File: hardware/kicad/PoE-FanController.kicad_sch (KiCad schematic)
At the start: 32 parts, among them J2 FAN1, J3 FAN2, J4 FAN3, J5 FAN4, J6 Molex_KK254_3pin, J8 Waveshare_ESP32P4POEETH, U1 LM2587-12

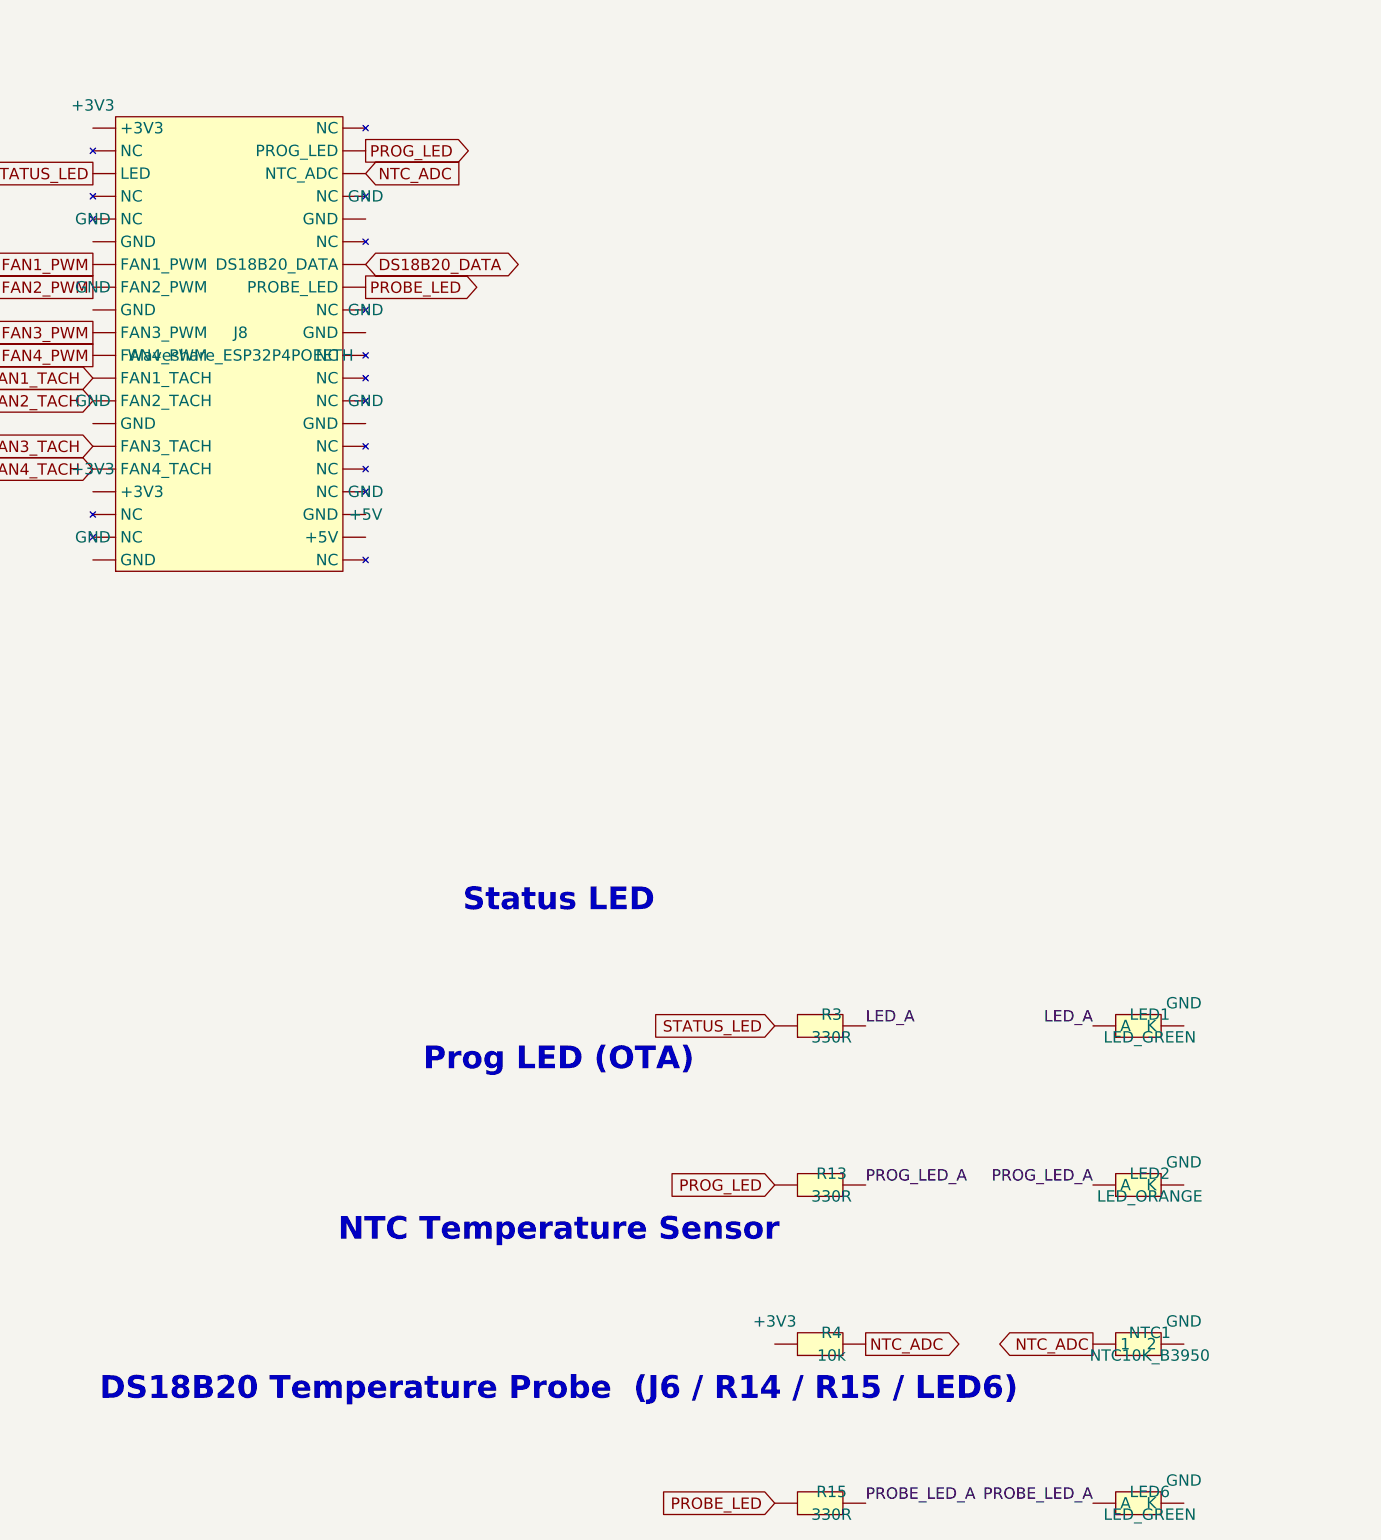
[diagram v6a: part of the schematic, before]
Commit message: feat(hw): replace NTC1/R4 with DHT11 breakout in schematic generator (#135)
- Remove Custom:NTC symbol definition from components.py
- Add Custom:DHT11_Breakout 3-pin symbol (VCC/DATA/GND)
- Remove R4 (NTC bias resistor) component and wiring
- Remove NTC1 thermistor component and wiring
- Add HUM1 (DHT11_Breakout) at same schematic row
- Rename NTC_ADC net to DHT11_DATA on J8 pin 23 (GPIO16)
- Update bom.py: remove R4/NTC1 rows, add HUM1 row
- ERC: 0 errors, 79 warnings (pre-existing)

Closes #135
Task: T001
Issue: #135

Co-authored-by: Copilot <223556219+Copilot@users.noreply.github.com>
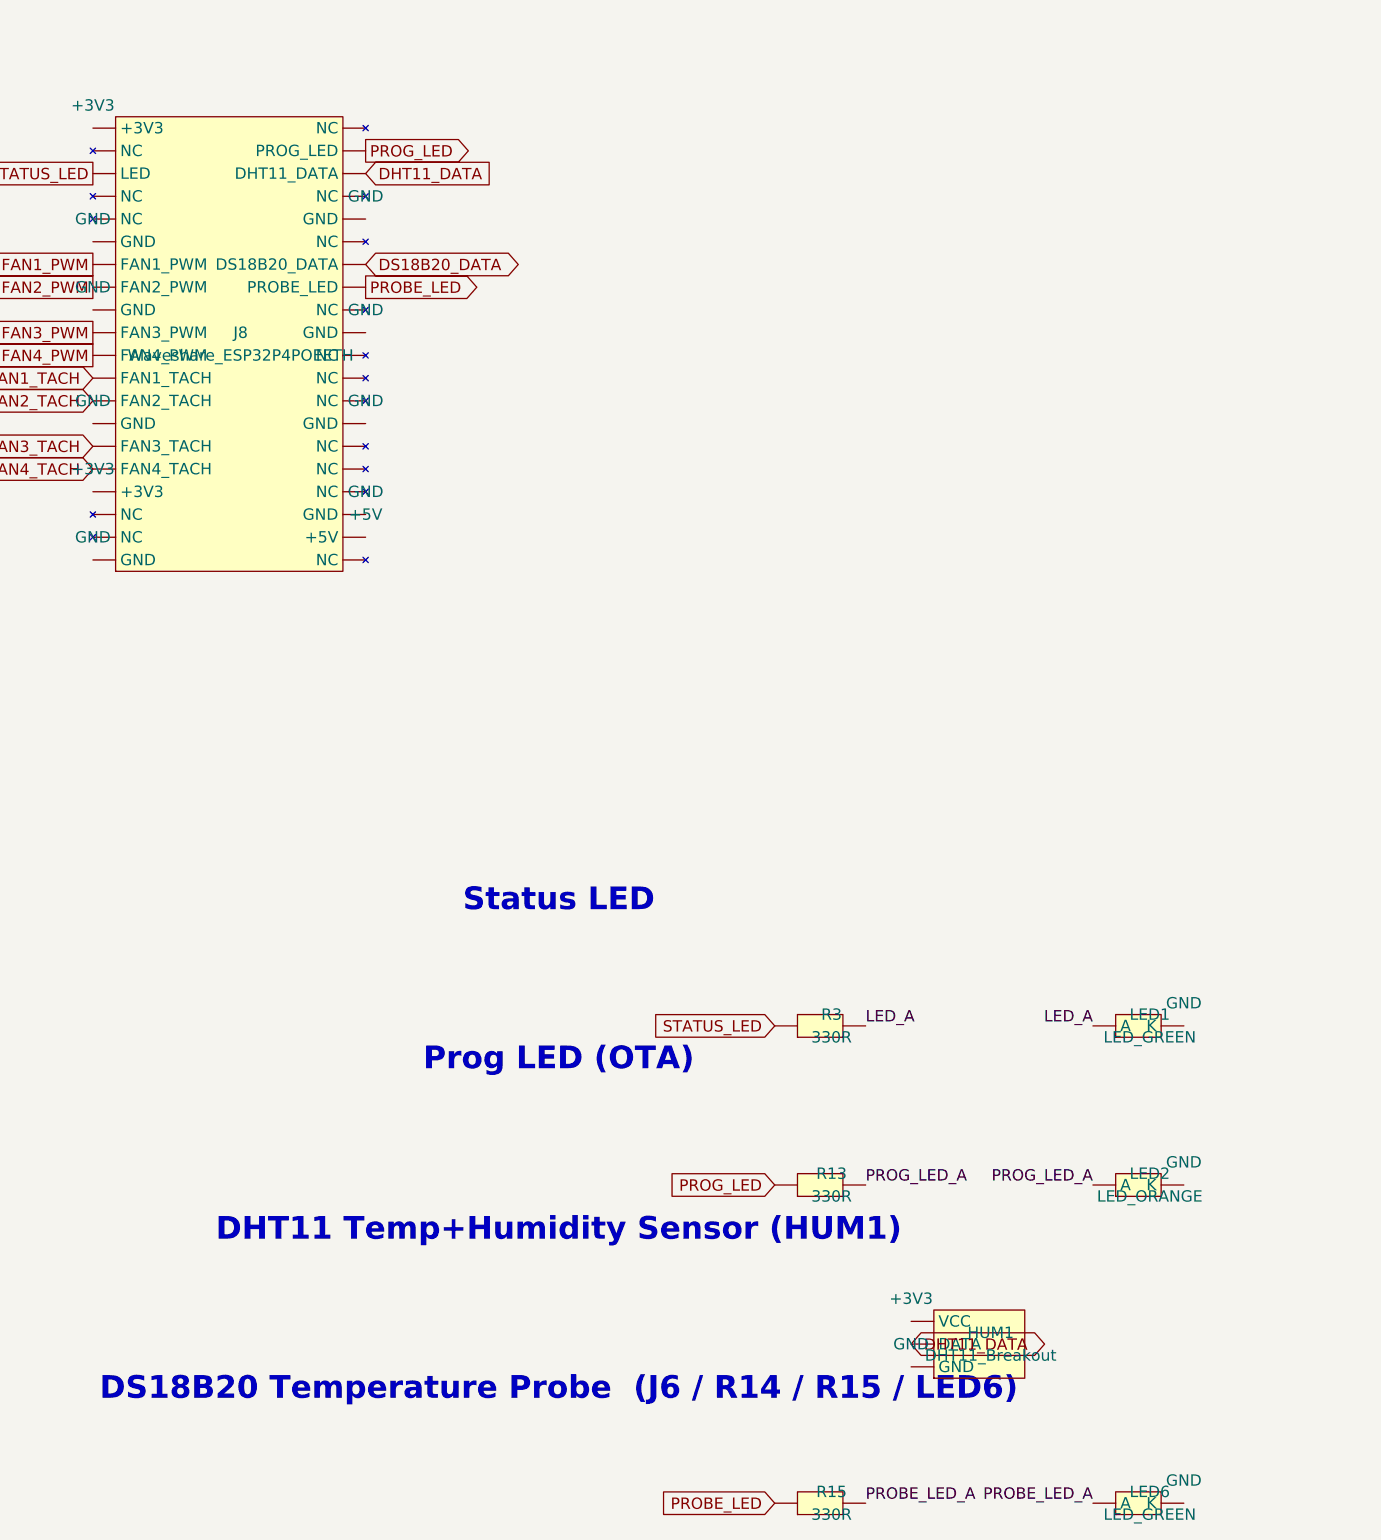
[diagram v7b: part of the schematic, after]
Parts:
- removed NTC1: NTC10K_B3950, Resistor_THT:R_Axial_DIN0207_L6.3mm_D2.5mm_P10.16mm_Horizontal, symbol Custom:NTC
- removed R4: 10k, Resistor_THT:R_Axial_DIN0207_L6.3mm_D2.5mm_P7.62mm_Horizontal, symbol Custom:R
- added HUM1: DHT11_Breakout, Connector_PinHeader_2.54mm:PinHeader_1x03_P2.54mm_Vertical, symbol Custom:DHT11_Breakout
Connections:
- net NTC_ADC renamed DHT11_DATA
- net DHT11_DATA: now also HUM1.2 (DATA)
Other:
- note added: "DHT11 Temp+Humidity Sensor (HUM1)"
- note removed: "NTC Temperature Sensor"
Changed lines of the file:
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@@
     (instances (project "PoE-FanController" (path "/" (reference "#PWR031") (unit 1))))
   )
-  (text "NTC Temperature Sensor" (at 128.2700 251.4600 0)
+  (text "DHT11 Temp+Humidity Sensor (HUM1)" (at 128.2700 251.4600 0)
     (effects (font (color 0 0 255 1) (bold yes) (size 2.54 2.54)))
 )
-  (symbol (lib_id "Custom:R") (at 157.4800 264.1600 0)
-    (unit 1) (exclude_from_sim no) (in_bom yes) (on_board yes) (dnp no)
-    (property "Reference" "R4"
-      (at 158.7500 262.8900 0)
-      (effects (font (size 1.27 1.27))))
-    (property "Value" "10k"
-      (at 158.7500 265.4300 0)
-      (effects (font (size 1.27 1.27))))
-    (property "Footprint" "Resistor_THT:R_Axial_DIN0207_L6.3mm_D2.5mm_P7.62mm_Horizontal"
-      (at 157.4800 264.1600 0)
+  (symbol (lib_id "Custom:DHT11_Breakout") (at 175.2600 264.1600 0)
+    (unit 1) (exclude_from_sim no) (in_bom yes) (on_board yes) (dnp no)
+    (property "Reference" "HUM1"
+      (at 176.5300 262.8900 0)
+      (effects (font (size 1.27 1.27))))
+    (property "Value" "DHT11_Breakout"
+      (at 176.5300 265.4300 0)
+      (effects (font (size 1.27 1.27))))
+    (property "Footprint" "Connector_PinHeader_2.54mm:PinHeader_1x03_P2.54mm_Vertical"
+      (at 175.2600 264.1600 0)
       (hide yes)
       (effects (font (size 1.27 1.27))))
     (property "Datasheet" "~"
-      (at 157.4800 264.1600 0)
+      (at 175.2600 264.1600 0)
       (hide yes)
       (effects (font (size 1.27 1.27))))
     (pin "1")
     (pin "2")
-    (instances (project "PoE-FanController" (path "/" (reference "R4") (unit 1))))
-  )
-  (symbol (lib_id "power:+3V3") (at 152.4000 264.1600 0)
+    (pin "3")
+    (instances (project "PoE-FanController" (path "/" (reference "HUM1") (unit 1))))
+  )
+  (symbol (lib_id "power:+3V3") (at 167.6400 261.6200 0)
     (unit 1) (exclude_from_sim no) (in_bom yes) (on_board yes) (dnp no)
     (fields_autoplaced yes)
     (property "Reference" "#PWR032"
-      (at 152.4000 266.7000 0)
+      (at 167.6400 264.1600 0)
       (hide yes)
       (effects (font (size 1.27 1.27))))
     (property "Value" "+3V3"
-      (at 152.4000 261.6200 0)
-      (effects (font (size 1.27 1.27))))
-    (property "Footprint" ""
-      (at 152.4000 264.1600 0)
-      (hide yes)
-      (effects (font (size 1.27 1.27))))
-    (property "Datasheet" ""
-      (at 152.4000 264.1600 0)
+      (at 167.6400 259.0800 0)
+      (effects (font (size 1.27 1.27))))
+    (property "Footprint" ""
+      (at 167.6400 261.6200 0)
+      (hide yes)
+      (effects (font (size 1.27 1.27))))
+    (property "Datasheet" ""
+      (at 167.6400 261.6200 0)
       (hide yes)
       (effects (font (size 1.27 1.27))))
@@
     (instances (project "PoE-FanController" (path "/" (reference "#PWR032") (unit 1))))
   )
-  (global_label "NTC_ADC"
-    (shape output)
-    (at 162.5600 264.1600 0)
+  (global_label "DHT11_DATA"
+    (shape bidirectional)
+    (at 167.6400 264.1600 0)
     (fields_autoplaced yes)
     (effects (font (size 1.27 1.27)) (justify left))
     (property "Intersheetrefs" "${INTERSHEET_REFS}"
-      (at 170.1800 264.1600 0)
+      (at 175.2600 264.1600 0)
       (effects (font (size 1.27 1.27)) (justify left) (hide yes)))
   )
-  (symbol (lib_id "Custom:NTC") (at 193.0400 264.1600 0)
-    (unit 1) (exclude_from_sim no) (in_bom yes) (on_board yes) (dnp no)
-    (property "Reference" "NTC1"
-      (at 194.3100 262.8900 0)
-      (effects (font (size 1.27 1.27))))
-    (property "Value" "NTC10K_B3950"
-      (at 194.3100 265.4300 0)
-      (effects (font (size 1.27 1.27))))
-    (property "Footprint" "Resistor_THT:R_Axial_DIN0207_L6.3mm_D2.5mm_P10.16mm_Horizontal"
-      (at 193.0400 264.1600 0)
-      (hide yes)
-      (effects (font (size 1.27 1.27))))
-    (property "Datasheet" "~"
-      (at 193.0400 264.1600 0)
-      (hide yes)
-      (effects (font (size 1.27 1.27))))
-    (pin "1")
-    (pin "2")
-    (instances (project "PoE-FanController" (path "/" (reference "NTC1") (unit 1))))
-  )
-  (global_label "NTC_ADC"
-    (shape output)
-    (at 187.9600 264.1600 180)
-    (fields_autoplaced yes)
-    (effects (font (size 1.27 1.27)) (justify right))
-    (property "Intersheetrefs" "${INTERSHEET_REFS}"
-      (at 195.5800 264.1600 180)
-      (effects (font (size 1.27 1.27)) (justify right) (hide yes)))
-  )
-  (symbol (lib_id "power:GND") (at 198.1200 264.1600 0)
+  (symbol (lib_id "power:GND") (at 167.6400 266.7000 0)
     (unit 1) (exclude_from_sim no) (in_bom yes) (on_board yes) (dnp no)
     (fields_autoplaced yes)
     (property "Reference" "#PWR033"
-      (at 198.1200 266.7000 0)
-      (hide yes)
-      (effects (font (size 1.27 1.27))))
-    (property "Value" "GND"
-      (at 198.1200 261.6200 0)
-      (effects (font (size 1.27 1.27))))
-    (property "Footprint" ""
-      (at 198.1200 264.1600 0)
-      (hide yes)
-      (effects (font (size 1.27 1.27))))
-    (property "Datasheet" ""
-      (at 198.1200 264.1600 0)
+      (at 167.6400 269.2400 0)
+      (hide yes)
+      (effects (font (size 1.27 1.27))))
+    (property "Value" "GND"
+      (at 167.6400 264.1600 0)
+      (effects (font (size 1.27 1.27))))
+    (property "Footprint" ""
+      (at 167.6400 266.7000 0)
+      (hide yes)
+      (effects (font (size 1.27 1.27))))
+    (property "Datasheet" ""
+      (at 167.6400 266.7000 0)
       (hide yes)
       (effects (font (size 1.27 1.27))))
@@
       (effects (font (size 1.27 1.27)) (justify left) (hide yes)))
   )
-  (global_label "NTC_ADC"
+  (global_label "DHT11_DATA"
     (shape input)
     (at 106.6800 133.3500 0)

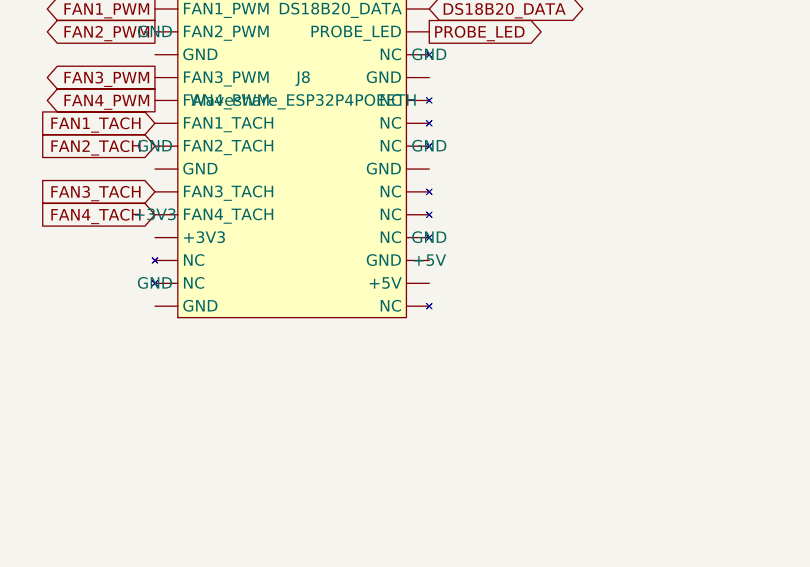
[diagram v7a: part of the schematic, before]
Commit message: hw(sch): move 5V power source from J8 pin 39 (VSYS) to pin 40 (VBUS) (#138)
* hw(sch): move 5V power source from J8 pin 39 (VSYS) to pin 40 (VBUS)

- components.py: pin 39 -> NC (VSYS), pin 40 -> +5V (VBUS)
- Schematic regenerated via python hardware/generate_project.py
- ERC: 0 errors, 79 acceptable warnings (single-label globals, multi-junction)
- DRC: 0 errors, 70 unconnected (pre-existing unrouted ratsnest, unchanged)
- PCB netlist sync (F8) required in KiCad GUI — see next commit

Closes #137

Co-authored-by: Copilot <223556219+Copilot@users.noreply.github.com>

* hw(pcb): sync netlist — J8 pad 39 -> NC, pad 40 -> +5V (VBUS)

Applied via pcbnew Python pad net reassignment (equivalent to F8 in GUI).
DRC: 0 errors, 16 silk warnings, 70 unconnected (pre-existing unrouted ratsnest).

Co-authored-by: Copilot <223556219+Copilot@users.noreply.github.com>

* chore(skills): add kikit-netlist-sync skill

Scripted equivalent of KiCad GUI F8 (Update PCB from Schematic).
Reassigns pad nets via pcbnew Python API — no GUI required.

Co-authored-by: Copilot <223556219+Copilot@users.noreply.github.com>

* fix(sch): complete pin 39->40 migration in generator and regenerate schematic

The schematic generator (components.py) still had s.power('+5V', *p['39'])
which caused 2 ERC errors (pin_not_connected) in CI.

- components.py: move s.power('+5V') call from p['39'] to p['40']
- Update all comments to reflect VSYS=NC, VBUS=+5V
- Regenerate schematic via python hardware/generate_project.py
- ERC (JSON): 0 errors ✅ (79 acceptable warnings)
- PCB pads already correct from previous netlist sync commit

Co-authored-by: Copilot <223556219+Copilot@users.noreply.github.com>

---------

Co-authored-by: Copilot <223556219+Copilot@users.noreply.github.com>
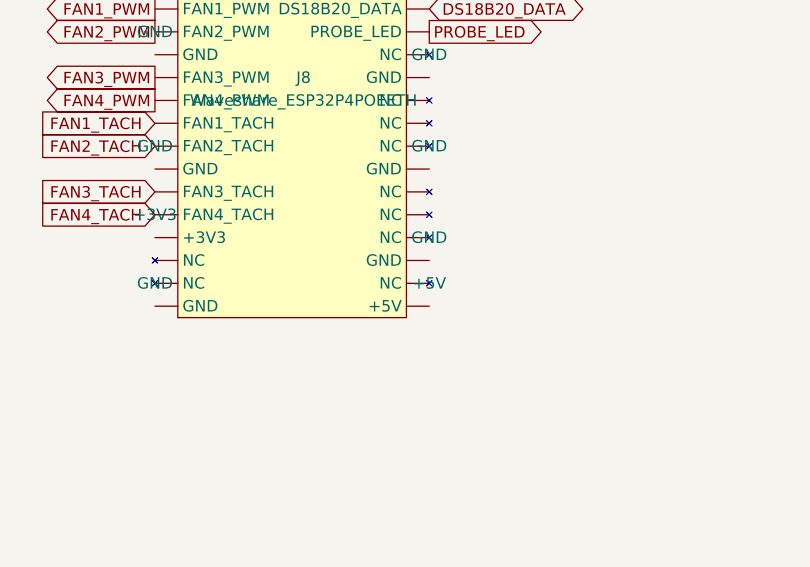
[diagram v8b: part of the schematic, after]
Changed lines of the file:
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@@
     (instances (project "PoE-FanController" (path "/" (reference "#PWR047") (unit 1))))
   )
-  (symbol (lib_id "power:+5V") (at 106.6800 173.9900 0)
+  (symbol (lib_id "power:+5V") (at 106.6800 176.5300 0)
     (unit 1) (exclude_from_sim no) (in_bom yes) (on_board yes) (dnp no)
     (fields_autoplaced yes)
     (property "Reference" "#PWR048"
+      (at 106.6800 179.0700 0)
+      (hide yes)
+      (effects (font (size 1.27 1.27))))
+    (property "Value" "+5V"
+      (at 106.6800 173.9900 0)
+      (effects (font (size 1.27 1.27))))
+    (property "Footprint" ""
       (at 106.6800 176.5300 0)
       (hide yes)
       (effects (font (size 1.27 1.27))))
-    (property "Value" "+5V"
-      (at 106.6800 171.4500 0)
-      (effects (font (size 1.27 1.27))))
-    (property "Footprint" ""
-      (at 106.6800 173.9900 0)
+    (property "Datasheet" ""
+      (at 106.6800 176.5300 0)
       (hide yes)
       (effects (font (size 1.27 1.27))))
-    (property "Datasheet" ""
-      (at 106.6800 173.9900 0)
-      (hide yes)
-      (effects (font (size 1.27 1.27))))
